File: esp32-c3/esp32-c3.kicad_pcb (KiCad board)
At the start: 4 copper layers, 80 x 40 mm, 62 parts, among them J1 Conn_01x04_Socket, J2 USB_C_Receptacle_USB2.0_16P, J3 Conn_01x02_Pin, J4 Conn_01x02_Pin, J5 Conn_01x02_Pin, Q1 SS8050, Q2 SS8050, U1 ESP32-C3-MINI-1, U3 CPS125, U4 CP2102N-Axx-xQFN28, U5 AMS1117-3.3, U6 TPS5430DDA, U7 TC118S, U8 TC118S, U9 M24C02-RMN

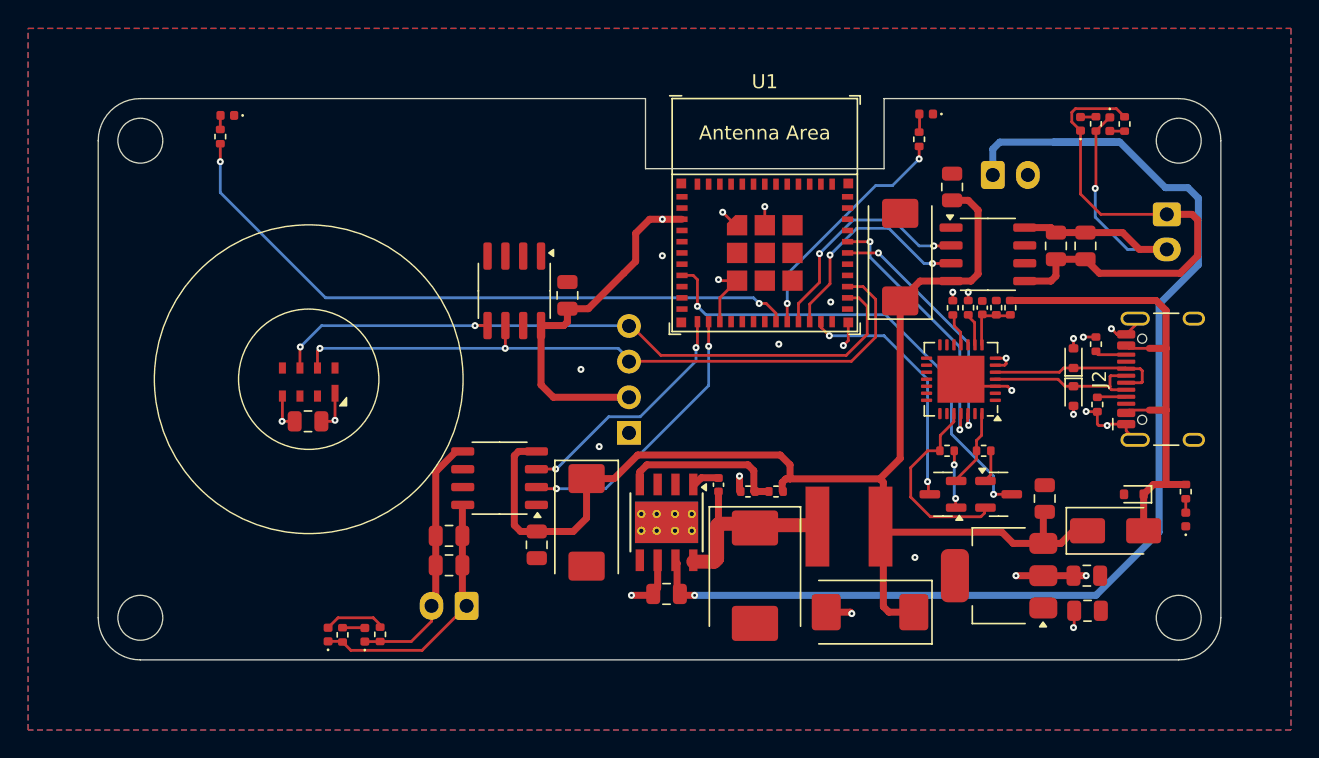
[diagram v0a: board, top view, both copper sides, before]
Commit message: Fix Battery power and USB/UART connection, move vent around to accomodate enclosure
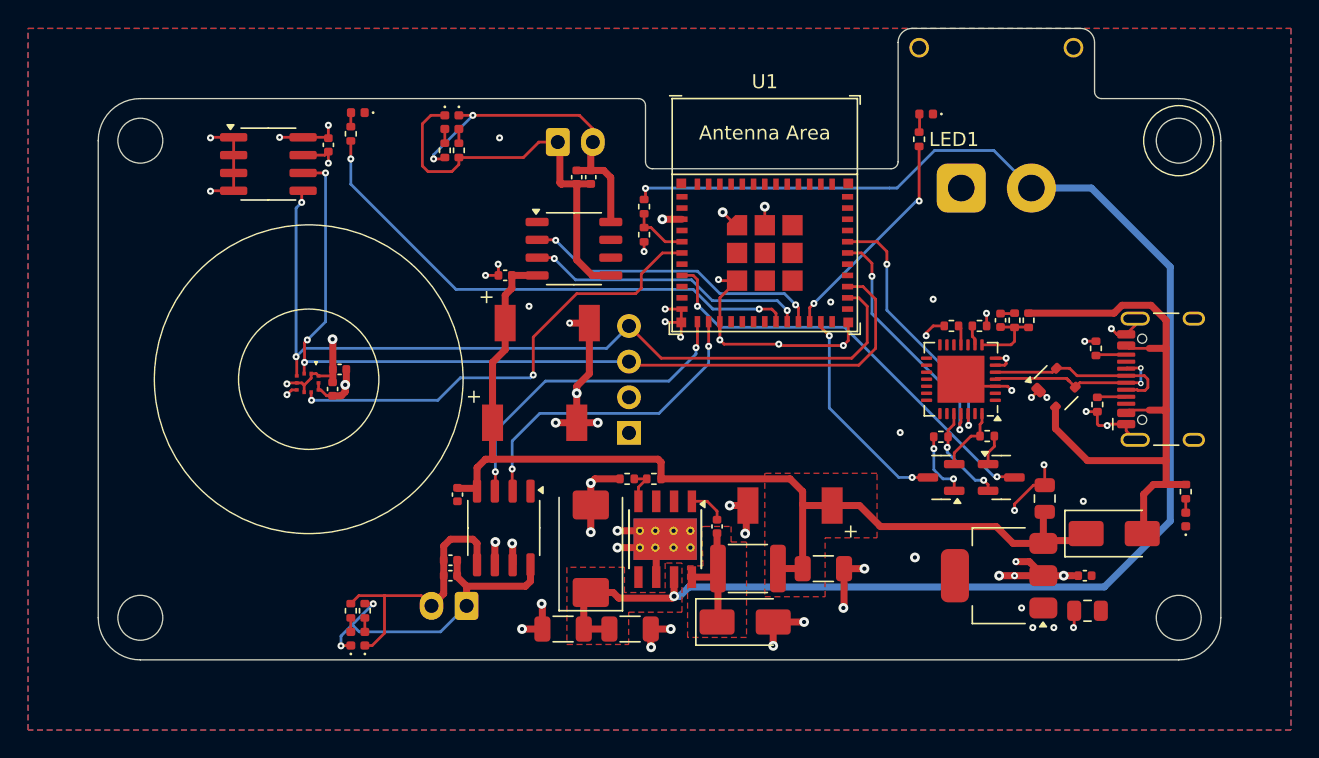
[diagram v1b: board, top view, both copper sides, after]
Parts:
- removed C6: 10uF, Capacitor_SMD:C_0805_2012Metric
- removed C7: 10nF, Capacitor_SMD:C_0402_1005Metric
- removed C8: 220uF, Capacitor_Tantalum_SMD:CP_EIA-7343-43_Kemet-X
- removed D3, D4, D5: LESD5D5.0CT1G-ES, Diode_SMD:D_SOD-523
- removed L1: SWPA6028S180MT, inductor:Inductor_6x6mm
- removed R12, R13: 10K, Resistor_SMD:R_0402_1005Metric
- removed U3: CPS125, local:CPS125
- removed U6: TPS5430DDA, Package_SO:TI_SO-PowerPAD-8_ThermalVias
- added C18: 100nF, Capacitor_SMD:C_0402_1005Metric, F.Cu at (142.2, 89.3)
- added C301: 10uF, Capacitor_SMD:C_1206_3216Metric, F.Cu at (162.9, 107.8)
- added C302: EEFCX0J221YR, local:CP_SMD_4.3x7.3mm, F.Cu at (174.3, 99.0)
- added C303: 220uF, Capacitor_Tantalum_SMD:CP_EIA-7343-31_Kemet-D, F.Cu at (160.1, 102.1)
- added C310: 10uF, Capacitor_SMD:C_1206_3216Metric, F.Cu at (158.1, 107.8)
- added C311: 10nF, Capacitor_SMD:C_0402_1005Metric, F.Cu at (169.1, 100.5)
- added C312: 10uF, Capacitor_SMD:C_1206_3216Metric, F.Cu at (176.7, 103.5)
- added D301: B340A, Diode_SMD:D_SMA, F.Cu at (171.1, 107.3)
- added L301: FHW1812IF1R8JST, Inductor_SMD:L_1812_4532Metric, F.Cu at (171.3, 103.5)
- added R18: 1K, Resistor_SMD:R_0402_1005Metric, F.Cu at (163.9, 79.7)
- added R19: 10K, Resistor_SMD:R_0402_1005Metric, F.Cu at (163.9, 77.7)
- added R301: 10k, Resistor_SMD:R_0402_1005Metric, F.Cu at (164.6, 97.1)
- added R302: 3k24, Resistor_SMD:R_0402_1005Metric, F.Cu at (162.7, 97.1)
- added U2: BMP580, local:BMP580_FP, F.Cu at (139.9, 90.3)
- added U301: TPS5430DDA, Package_SO:TI_SO-PowerPAD-8_ThermalVias, F.Cu at (165.4, 101.4)
- C1, C10, C11, C12, C14, C15, C16, C17, C5: footprint Capacitor_SMD:C_0805_2012Metric -> Capacitor_SMD:C_0402_1005Metric
- C13, C9: value 220uF -> EEFCX0J221YR; footprint Capacitor_Tantalum_SMD:CP_EIA-7343-43_Kemet-X -> local:CP_SMD_4.3x7.3mm
- D8: value B340 -> SP0503BAHT; footprint Diode_SMD:D_SMC -> Package_TO_SOT_SMD:SOT-143
- J3: footprint Connector_JST:JST_XH_S2B-XH-A_1x02_P2.50mm_Horizontal -> Connector_AMASS:AMASS_XT30PW-M_1x02_P2.50mm_Horizontal
- R6: value 46.5K -> 43K
- moved R15 47.5 mm to (150.7, 73.7), turned to -90 degrees
- moved R14 46.4 mm to (149.7, 73.7)
- moved D10 46.4 mm to (150.7, 71.7)
- moved D9 45.3 mm to (149.7, 71.7), turned to -90 degrees
- moved J4 43.7 mm to (157.8, 73.1), turned to 0 degrees
- moved C11 35.6 mm to (160.1, 75.6)
- moved C12 34.5 mm to (159.1, 75.6)
- moved C10 32.5 mm to (154.0, 82.6), turned to 180 degrees
- moved U7 29.5 mm to (158.9, 80.7)
- moved C9 25.6 mm to (157.0, 86.0), turned to 0 degrees
- moved D8 25.3 mm to (193.2, 90.6), turned to 45 degrees
- moved C17 20.1 mm to (141.4, 73.3), turned to -90 degrees
- moved U9 19.7 mm to (137.1, 74.7), turned to 0 degrees
- moved D2 9.30 mm to (143.5, 71.0)
- moved R4 9.30 mm to (143.0, 72.5)
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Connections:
- D8 pad 1: Net-(D8-K) -> GND
- D8 pad 2: GND -> +5VP
- J3 pad 1: +7.5V -> GND
- J3 pad 2: GND -> +7.5V
- U1 pad 20: /LED1 -> /MTR1
- U1 pad 22: /MTR1 -> /LED1
- U1 pad 30: /UART_TX -> /UART_RX
- U1 pad 31: /UART_RX -> /UART_TX
- U1 pad 5: unconnected-(U1-GPIO2/ADC1_CH2-Pad5) -> /BatDiv10
- U1 pad 6: unconnected-(U1-GPIO3/ADC1_CH3-Pad6) -> /nINT
- U4 pad 4: /USB_UART/USB_DM -> /USB_UART/USB_DP
- U4 pad 5: /USB_UART/USB_DP -> /USB_UART/USB_DM
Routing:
- net GND: track 33.9 -> 107.2 mm, vias 22 -> 57
- net /nINT: track 0.00 -> 33.5 mm, vias 0 -> 2
- net +7.5V: track 88.7 -> 110.6 mm, vias 1 -> 2
- net +5V: track 94.5 -> 75.2 mm
- net /SCL: track 48.7 -> 63.7 mm, vias 2 -> 3
- net Net-(D8-K): track 13.8 -> 0.00 mm
- net +3.3V: track 38.6 -> 25.6 mm, vias 7 -> 12
- net /SDA: track 48.4 -> 60.7 mm
- net Net-(U6-VSENSE): track 12.0 -> 0.00 mm
- net /LED0: track 46.9 -> 37.5 mm
- net +5VP: track 36.5 -> 45.5 mm
- net /Battery/5Vvar: track 0.00 -> 8.24 mm
- net /Motor/Mot_b: track 36.5 -> 29.4 mm
- net /RTS: track 14.1 -> 7.26 mm, vias 0 -> 2
- net /Vent1: track 17.4 -> 23.2 mm
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- added copper zone on F.Cu, net +5V
- added copper zone on F.Cu, net +7.5V
- added copper zone on F.Cu, net /Battery/5Vvar
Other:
- board size 80 x 40 mm -> 80 x 45 mm
- board text added: "7.5V"
- board text added: "ESP32C3 based Blowpipe adapter 20250523"
- board text added: "LED1"
- board text added: "SDA SCL 3.3V GND"
